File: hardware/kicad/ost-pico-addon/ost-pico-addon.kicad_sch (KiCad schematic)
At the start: 7 parts, among them J1 Conn_01x09_Male, J2 104031-0811, J3 Conn_01x08_Male, J4 Conn_01x03_Male, U1 Pico

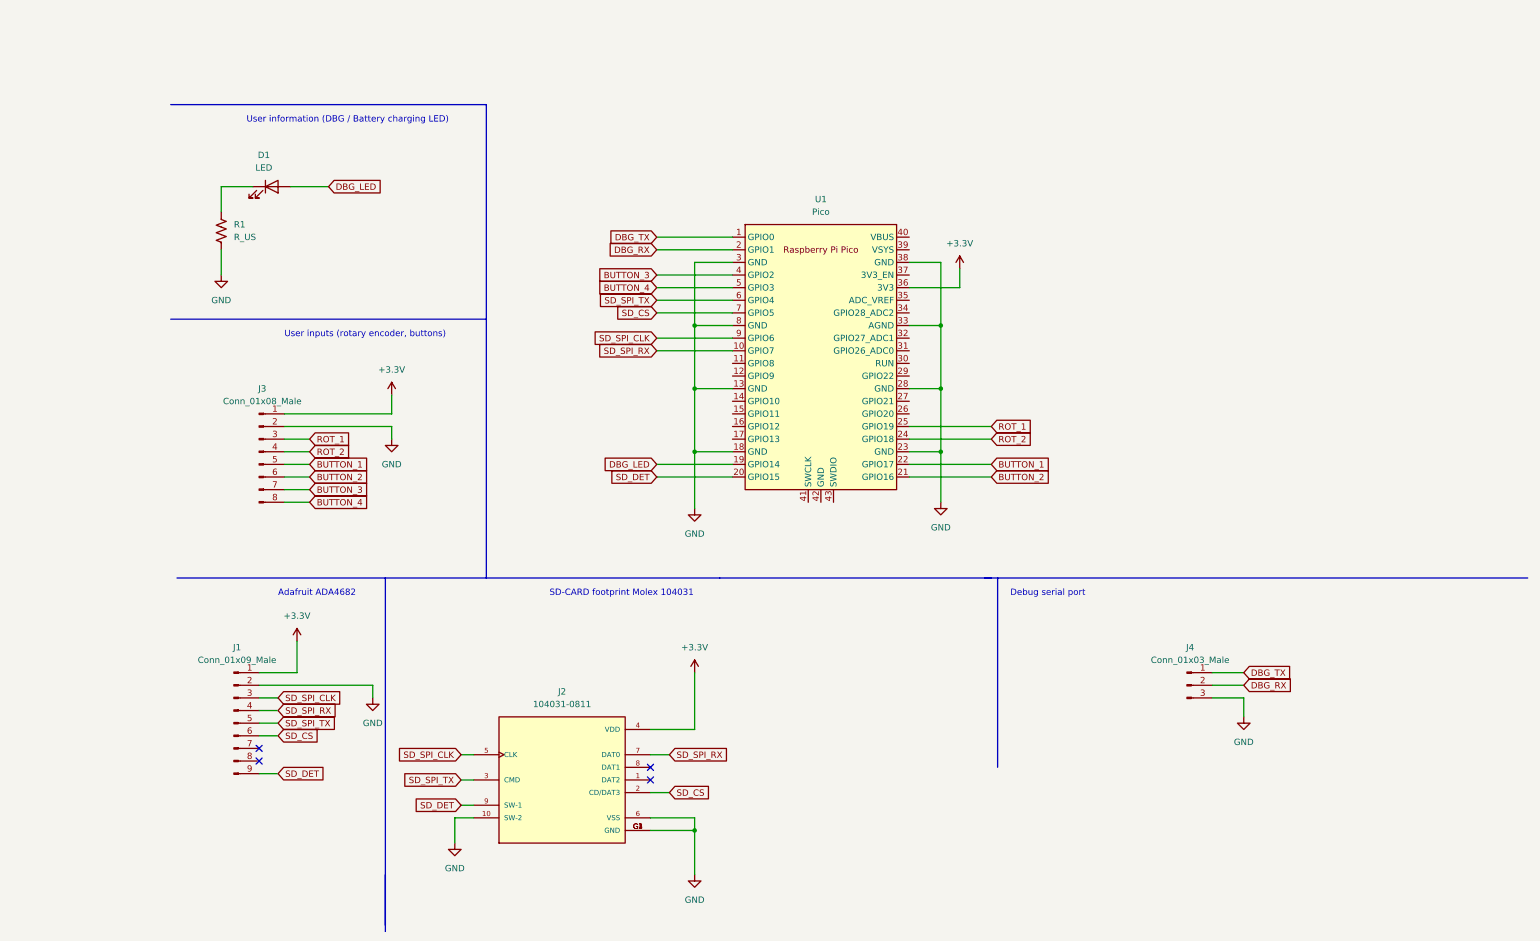
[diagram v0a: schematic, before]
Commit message: pinout and routing changes
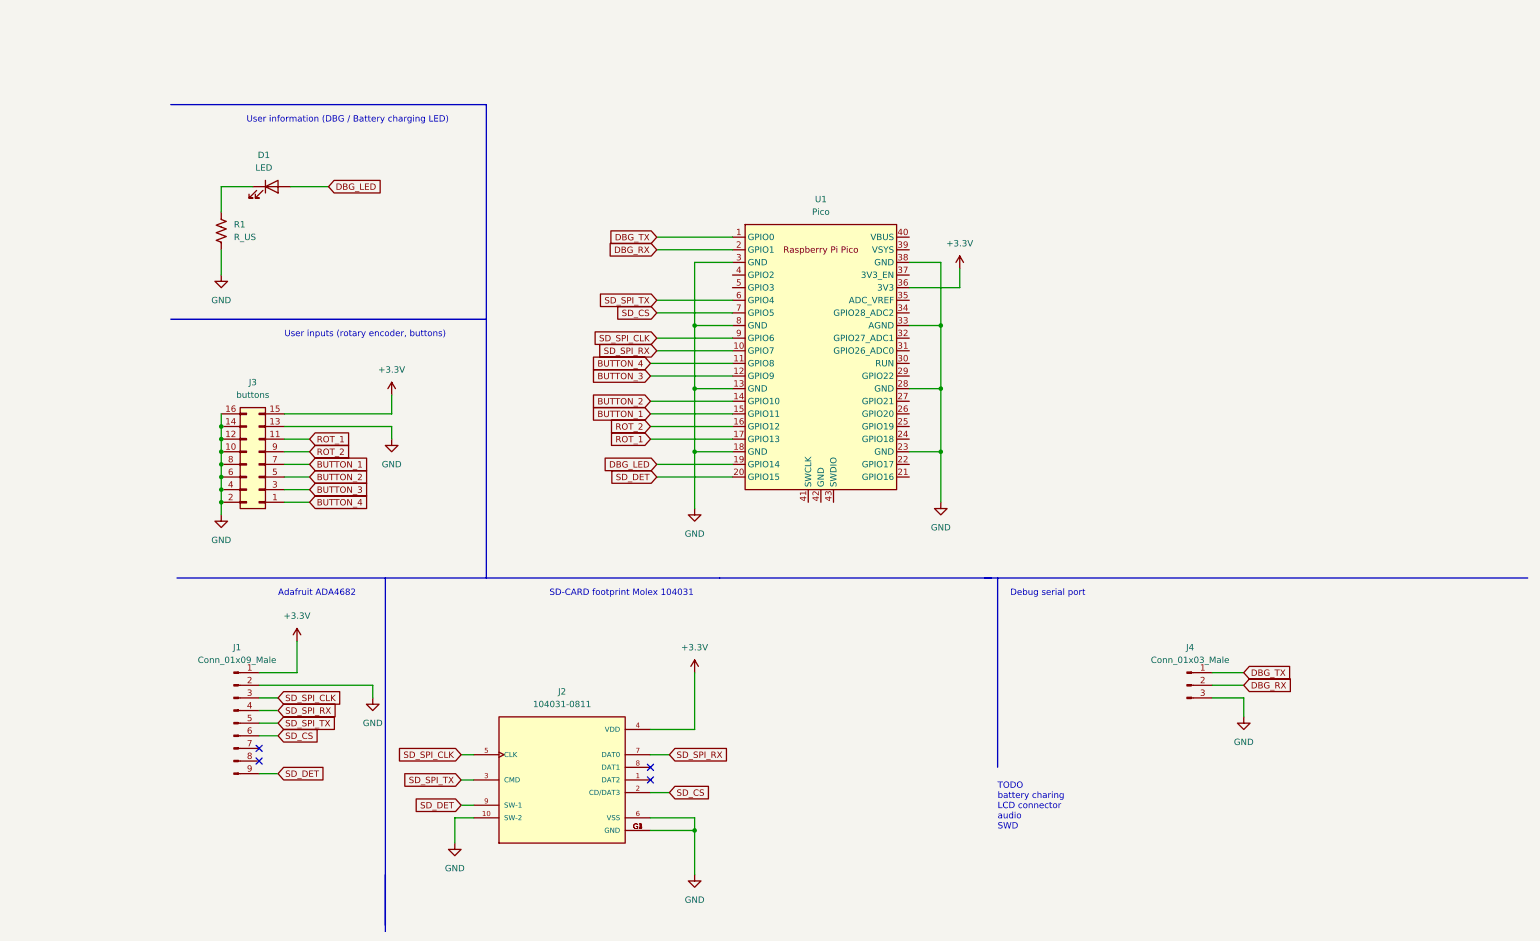
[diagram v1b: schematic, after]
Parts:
- removed J3: Conn_01x08_Male, Connector_PinHeader_2.54mm:PinHeader_1x08_P2.54mm_Vertical, symbol Connector:Conn_01x08_Male
- added J3: buttons, Connector_PinSocket_2.54mm:PinSocket_2x08_P2.54mm_Vertical, symbol Connector_Generic:Conn_02x08_Odd_Even
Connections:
- net +3.3V: now also J3.15 (Pin_15)
- net BUTTON_1: now also U1.15 (GPIO11), J3.7 (Pin_7); no longer U1.22 (GPIO17)
- net BUTTON_2: now also U1.14 (GPIO10), J3.5 (Pin_5); no longer U1.21 (GPIO16)
- net BUTTON_3: now also U1.12 (GPIO9), J3.3 (Pin_3); no longer U1.4 (GPIO2)
- net BUTTON_4: now also U1.11 (GPIO8), J3.1 (Pin_1); no longer U1.5 (GPIO3)
- net GND: now also J3.10 (Pin_10), J3.12 (Pin_12), J3.13 (Pin_13), J3.14 (Pin_14), J3.16 (Pin_16), J3.2 (Pin_2), J3.4 (Pin_4), J3.6 (Pin_6), J3.8 (Pin_8)
- net ROT_1: now also U1.17 (GPIO13), J3.11 (Pin_11); no longer U1.25 (GPIO19)
- net ROT_2: now also U1.16 (GPIO12), J3.9 (Pin_9); no longer U1.24 (GPIO18)
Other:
- note added: "TODO battery charing LCD connector audio SWD"

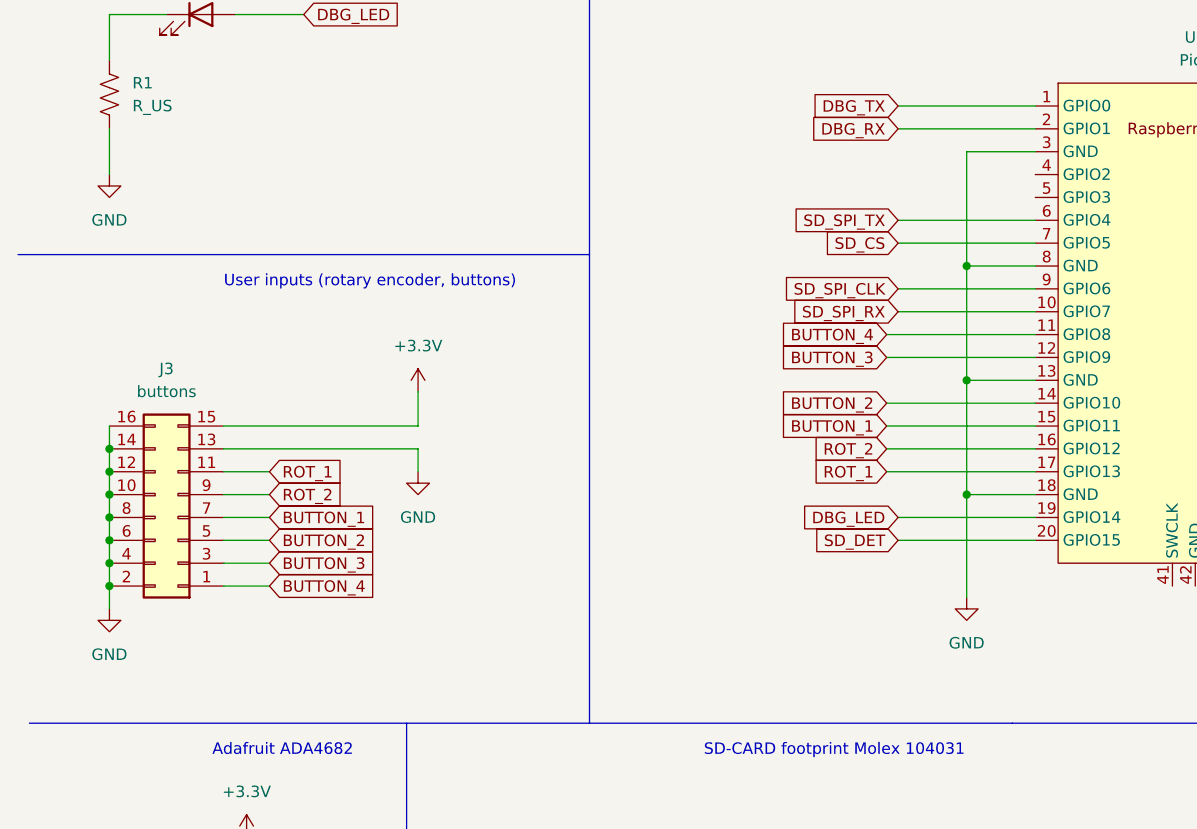
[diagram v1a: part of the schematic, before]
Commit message: change button port pinout
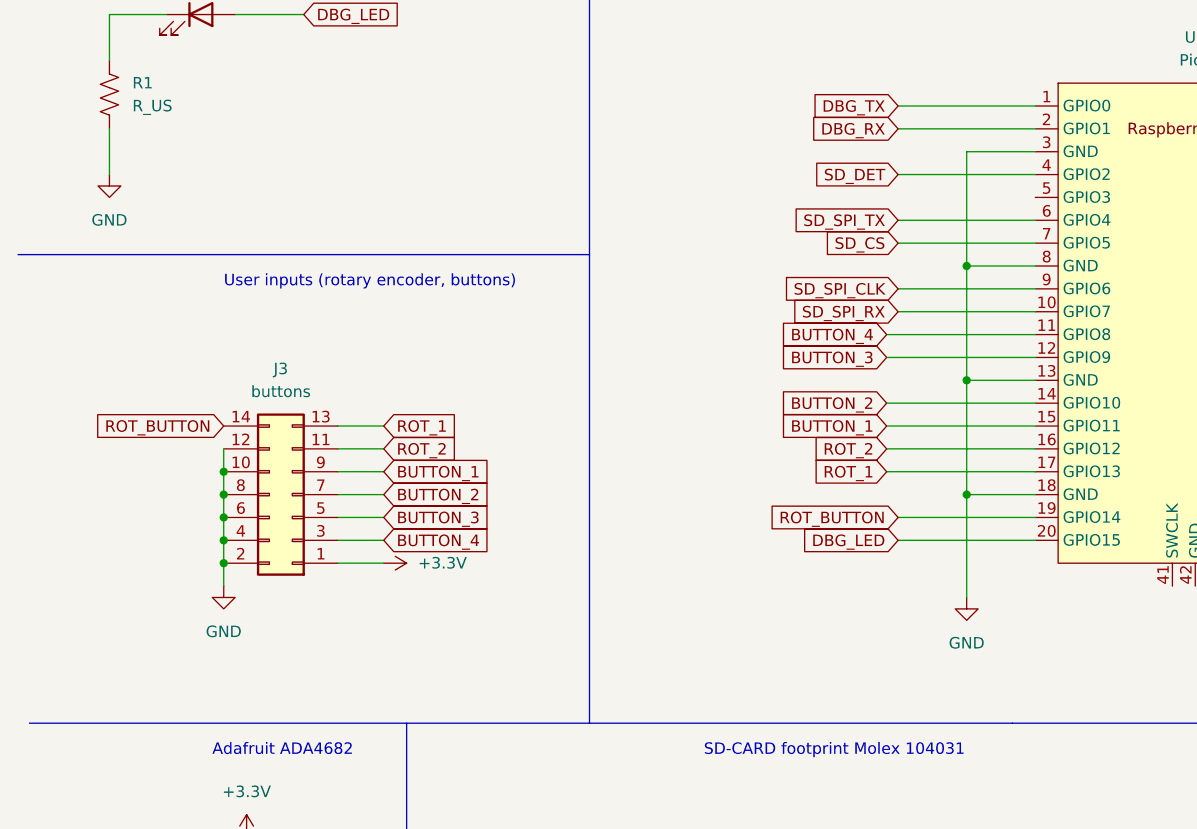
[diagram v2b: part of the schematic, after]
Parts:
- removed J3: buttons, Connector_PinSocket_2.54mm:PinSocket_2x08_P2.54mm_Vertical, symbol Connector_Generic:Conn_02x08_Odd_Even
- added J3: buttons, Connector_PinHeader_2.54mm:PinHeader_2x07_P2.54mm_Vertical, symbol Connector_Generic:Conn_02x07_Odd_Even
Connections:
- net +3.3V: now also J3.1 (Pin_1)
- net BUTTON_1: now also J3.9 (Pin_9)
- net BUTTON_2: now also J3.7 (Pin_7)
- net BUTTON_3: now also J3.5 (Pin_5)
- net BUTTON_4: now also J3.3 (Pin_3)
- net DBG_LED: now also U1.20 (GPIO15); no longer U1.19 (GPIO14)
- net GND: now also J3.10 (Pin_10), J3.12 (Pin_12), J3.2 (Pin_2), J3.4 (Pin_4), J3.6 (Pin_6), J3.8 (Pin_8)
- net ROT_1: now also J3.13 (Pin_13)
- net ROT_2: now also J3.11 (Pin_11)
- net SD_DET: now also U1.4 (GPIO2); no longer U1.20 (GPIO15)
- new net ROT_BUTTON: J3.14 (Pin_14), U1.19 (GPIO14)

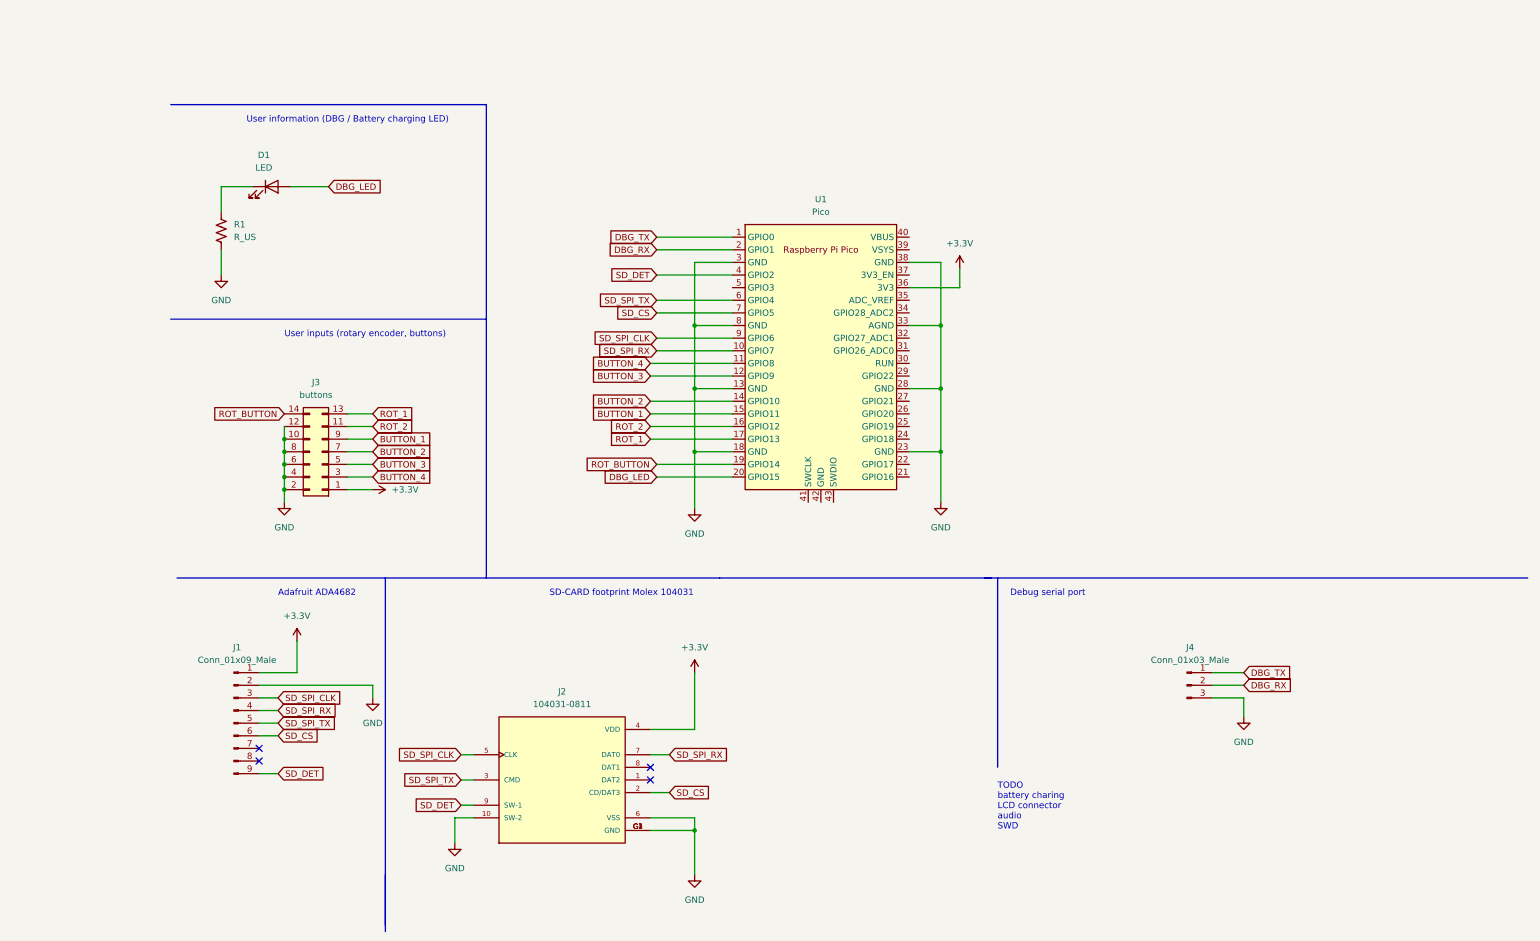
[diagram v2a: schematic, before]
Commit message: editor v2 + usb host tests
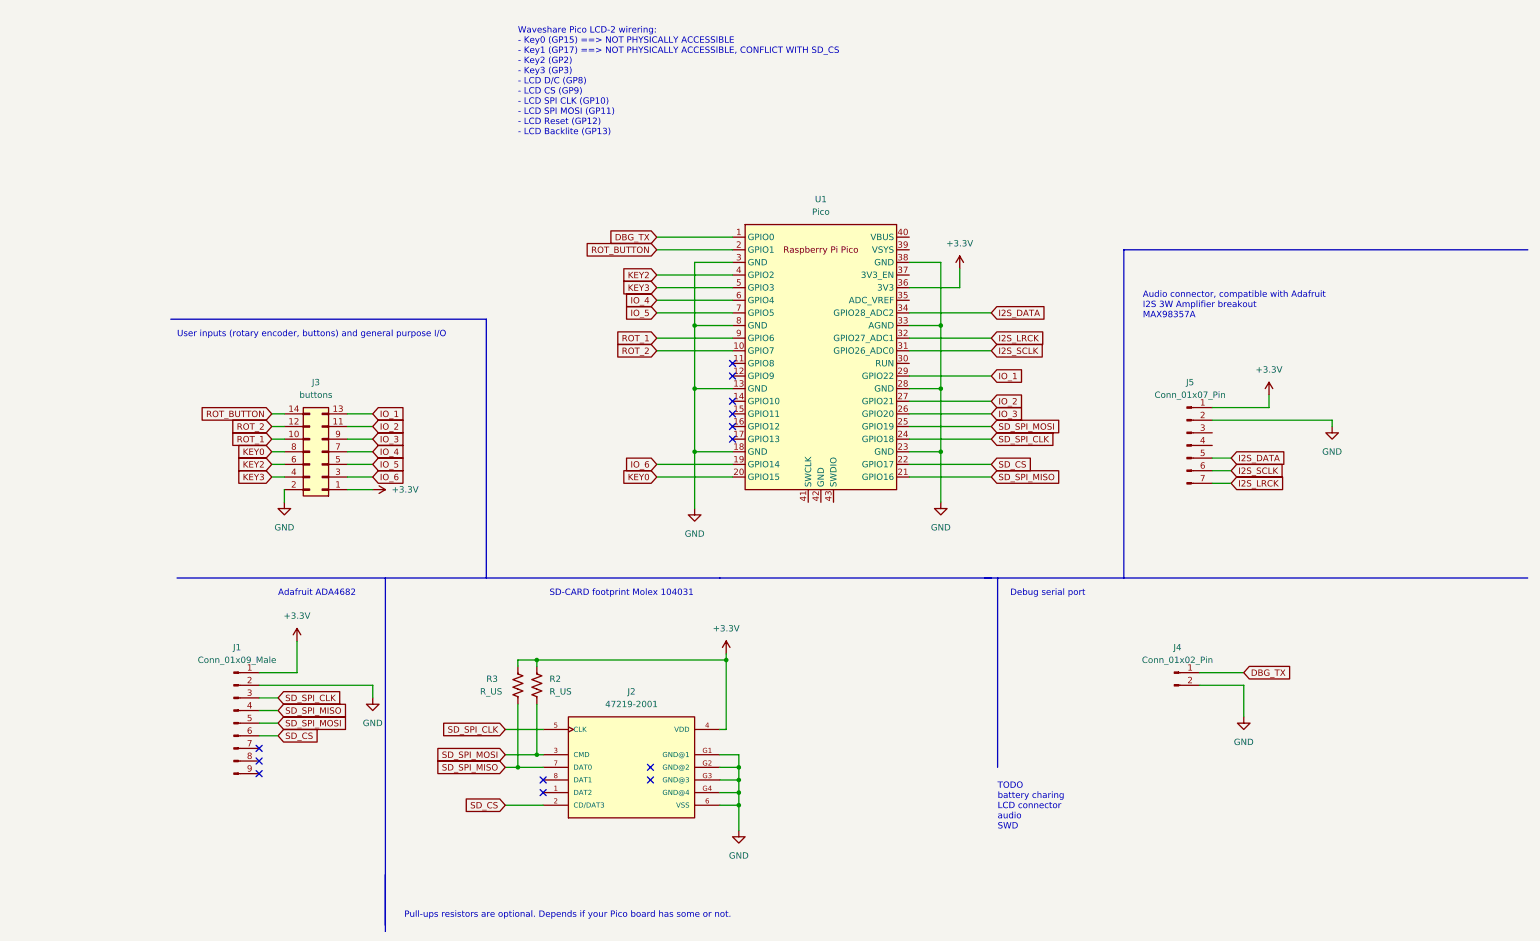
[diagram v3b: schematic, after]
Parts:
- removed D1: LED, LED_THT:LED_D3.0mm, symbol Device:LED
- removed J2: 104031-0811, Connector_Card:microSD_HC_Molex_104031-0811, symbol 104031-0811:104031-0811
- removed J4: Conn_01x03_Male, Connector_PinHeader_2.54mm:PinHeader_1x03_P2.54mm_Vertical, symbol Connector:Conn_01x03_Male
- removed R1: R_US, Resistor_THT:R_Axial_DIN0207_L6.3mm_D2.5mm_P10.16mm_Horizontal, symbol Device:R_US
- added J2: 47219-2001, sdcard-libs:MOLEX_47219-2001, symbol sdcard-libs:47219-2001
- added J4: Conn_01x02_Pin, Connector_PinHeader_2.54mm:PinHeader_1x02_P2.54mm_Vertical, symbol Connector:Conn_01x02_Pin
- added J5: Conn_01x07_Pin, Connector_PinHeader_2.54mm:PinHeader_1x07_P2.54mm_Vertical, symbol Connector:Conn_01x07_Pin
- added R2, R3: R_US, Resistor_THT:R_Axial_DIN0207_L6.3mm_D2.5mm_P10.16mm_Horizontal, symbol Device:R_US
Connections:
- net DBG_RX is gone; now on net ROT_BUTTON: U1.2 (GPIO1)
- net +3.3V: now also J2.4 (VDD), J5.1 (Pin_1), R2.1, R3.1
- net DBG_TX: now also J4.1 (Pin_1)
- net GND: now also J2.6 (VSS), J2.G1 (GND@1), J2.G2 (GND@2), J2.G3 (GND@3), J2.G4 (GND@4), J4.2 (Pin_2), J5.2 (Pin_2); no longer J3.10 (Pin_10), J3.12 (Pin_12), J3.4 (Pin_4), J3.6 (Pin_6), J3.8 (Pin_8)
- net ROT_1: now also J3.10 (Pin_10), U1.9 (GPIO6); no longer J3.13 (Pin_13), U1.17 (GPIO13)
- net ROT_2: now also J3.12 (Pin_12), U1.10 (GPIO7); no longer J3.11 (Pin_11), U1.16 (GPIO12)
- net ROT_BUTTON: no longer U1.19 (GPIO14)
- net SD_CS: now also U1.22 (GPIO17), J2.2 (CD/DAT3); no longer U1.7 (GPIO5)
- net SD_SPI_CLK: now also U1.24 (GPIO18), J2.5 (CLK); no longer U1.9 (GPIO6)
- net SD_SPI_MISO: now reaches U1.21 (GPIO16)
- net SD_SPI_MISO: now also J1.4 (Pin_4), J2.7 (DAT0), R3.2
- net SD_SPI_MOSI: now reaches U1.25 (GPIO19)
- net SD_SPI_MOSI: now also J1.5 (Pin_5), J2.3 (CMD), R2.2
- net IO_3: now reaches U1.26 (GPIO20)
- net IO_3: now also J3.9 (Pin_9)
- net IO_2: now reaches U1.27 (GPIO21)
- net IO_2: now also J3.11 (Pin_11)
- net IO_1: now reaches U1.29 (GPIO22)
- net IO_1: now also J3.13 (Pin_13)
- net I2S_SCLK: now reaches U1.31 (GPIO26_ADC0)
- net I2S_SCLK: now also J5.6 (Pin_6)
- net I2S_LRCK: now reaches U1.32 (GPIO27_ADC1)
- net I2S_LRCK: now also J5.7 (Pin_7)
- net I2S_DATA: now reaches U1.34 (GPIO28_ADC2)
- net I2S_DATA: now also J5.5 (Pin_5)
- net KEY3: now reaches U1.5 (GPIO3)
- net KEY3: now also J3.4 (Pin_4)
- net BUTTON_1: no longer names the net of U1.15 (GPIO11)
- net BUTTON_1: no longer J3.9 (Pin_9)
- net BUTTON_2: no longer names the net of U1.14 (GPIO10)
- net BUTTON_2: no longer J3.7 (Pin_7)
- net BUTTON_3: no longer names the net of U1.12 (GPIO9)
- net BUTTON_3: no longer J3.5 (Pin_5)
- net BUTTON_4: no longer names the net of U1.11 (GPIO8)
- net BUTTON_4: no longer J3.3 (Pin_3)
- net DBG_LED renamed KEY0
- net KEY0: now also J3.8 (Pin_8)
- net SD_DET: no longer names the net of J1.9 (Pin_9)
- net SD_DET: no longer U1.4 (GPIO2)
- removed net SD_SPI_RX: J1.4 (Pin_4), U1.10 (GPIO7)
- net SD_SPI_TX renamed IO_4
- net IO_4: now also J3.7 (Pin_7); no longer J1.5 (Pin_5)
- new net IO_5: J3.5 (Pin_5), U1.7 (GPIO5)
- new net IO_6: J3.3 (Pin_3), U1.19 (GPIO14)
- new net KEY2: J3.6 (Pin_6), U1.4 (GPIO2)
- no-connect marks 4 -> 13
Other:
- note added: "Audio connector, compatible with Adafruit I2S 3W Amplifier breakout MAX98357A"
- note added: "Pull-ups resistors are optional. Depends if your Pico board has some or not."
- note added: "User inputs (rotary encoder, buttons) and general purpose I/O"
- note added: "Waveshare Pico LCD-2 wirering: - Key0 (GP15) ==> NOT PHYSICALLY ACCESSIBLE - Key1 (GP17) ==> NOT PHYSICALLY ACCESSIBLE, CONFLICT WITH SD_CS - Key2 (GP2) - Key3 (GP3) - LCD D/C (GP8) - LCD CS (GP9) - LCD SPI CLK (GP10) - LCD SPI MOSI (GP11) - LCD Reset (GP12) - LCD Backlite (GP13)"
- note removed: "User information (DBG / Battery charging LED)"
- note removed: "User inputs (rotary encoder, buttons)"
